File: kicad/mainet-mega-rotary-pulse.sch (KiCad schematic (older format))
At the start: 11 parts, among them J65 Screw_Terminal_01x02, J66 Screw_Terminal_01x04, Q1 BUK9518-55, U1 4N38

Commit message: KICAD: Modificar sch del RPG
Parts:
- added J100, J99: Conn_01x01_Male, symbol Connector:Conn_01x01_Male
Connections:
- net labels removed: rotaryPulseOutput24V
- wire segments 30 -> 36
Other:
- note added: "+24V"
- note added: "Blanco"
- note added: "Esta señal es la salida a colector abierto\ndel RPG (Rotary Pulse Generator),\ngenerador de pulsos por rotación,\na 24VDC\n"
- note added: "Esta señal es la salida del generafor\nde pulsos por rotación trasladada a 5V.\nVa a la entrada D24 del Arduino-Mega"
- note added: "RPG"
- note added: "RPG Output"
- note added: "Rojo"
- note removed: "Esta señal es la salida del generador \nde pulsos por rotación a 24VDC\n"
- note removed: "Esta señal es la salida del generafor\nde pulsos por rotación trasladada a 5V"
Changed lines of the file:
@@
 $Descr A4 11693 8268
 encoding utf-8
-Sheet 21 22
+Sheet 22 22
 Title "Mainet-mega -- Convertidor de Voltaje: 24V a 5V"
 Date "2021-06-25"
@@
 Comment4 ""
 $EndDescr
-Text HLabel 3550 3750 2    50   Input ~ 0
-rotaryPulseOutput24V
+Text HLabel 6800 3600 2    50   Input ~ 0
+rotaryPulseOutput5V
 $Comp
 L Transistor_FET:IRLZ44N Q1
@@
 	6700 4050 6700 4450
 Connection ~ 6700 4450
-Text Label 7650 3600 2    50   ~ 0
-rotaryPulseOutput5V
 Text Label 6700 4450 0    50   ~ 0
 0V
-Text Notes 1350 3800 0    50   ~ 0
-Esta señal es la salida del generador \nde pulsos por rotación a 24VDC\n
-Text Notes 9100 3650 0    50   ~ 0
-Esta señal es la salida del generafor\nde pulsos por rotación trasladada a 5V
+Text Notes 3550 4300 0    50   ~ 0
+Esta señal es la salida a colector abierto\ndel RPG (Rotary Pulse Generator),\ngenerador de pulsos por rotación,\na 24VDC\n
+Text Notes 9150 3900 0    50   ~ 0
+Esta señal es la salida del generafor\nde pulsos por rotación trasladada a 5V.\nVa a la entrada D24 del Arduino-Mega
 $Comp
 L power:GNDD #PWR040
@@
 Wire Wire Line
 	4600 3050 5000 3050
+Text Notes 6500 5900 0    50   ~ 0
++24V
+Text Notes 3550 3750 0    50   ~ 0
++24V
+Text Notes 3550 3850 0    50   ~ 0
+RPG Output
+$Comp
+L Connector:Conn_01x01_Male J99
+U 1 1 60DC2EE7
+P 2600 3750
+F 0 "J99" H 2700 3650 50  0000 R CNN
+F 1 "Conn_01x01_Male" H 2572 3773 50  0001 R CNN
+F 2 "" H 2600 3750 50  0001 C CNN
+F 3 "~" H 2600 3750 50  0001 C CNN
+	1    2600 3750
+	-1   0    0    1
+$EndComp
+$Comp
+L Connector:Conn_01x01_Male J100
+U 1 1 60DC43F7
+P 2600 3850
+F 0 "J100" H 2750 3950 50  0000 R CNN
+F 1 "Conn_01x01_Male" H 2572 3873 50  0001 R CNN
+F 2 "" H 2600 3850 50  0001 C CNN
+F 3 "~" H 2600 3850 50  0001 C CNN
+	1    2600 3850
+	-1   0    0    1
+$EndComp
+Wire Notes Line
+	800  3900 1700 3900
+Wire Notes Line
+	1700 3900 1700 4700
+Wire Notes Line
+	1700 4700 800  4700
+Wire Notes Line
+	800  4700 800  3900
+Text Notes 900  4000 0    50   ~ 0
+RPG
+Wire Wire Line
+	1250 3900 1250 3750
+Wire Wire Line
+	1250 3750 2400 3750
+Wire Wire Line
+	2400 3850 1850 3850
+Wire Wire Line
+	1850 3850 1850 4250
+Wire Wire Line
+	1850 4250 1550 4250
+Wire Wire Line
+	1250 4700 1250 4850
+Text Notes 1850 3750 0    50   ~ 0
+Rojo
+Text Notes 1850 3850 0    50   ~ 0
+Blanco
 $EndSCHEMATC

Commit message: KICAD: Actualizar archivos sch
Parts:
- added J102: Conector del RPG, symbol Connector:Screw_Terminal_01x04
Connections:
- net labels added: +24V, GNDREF
- no-connect marks 1 -> 2
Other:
- note added: "Negro"
- note added: "Puede ser cualquiera de las salidas de +5V del Arduino-Mega"
- note removed: "No es la salida de +5V del Arduino"
- note removed: "RPG"
- moved on the sheet: D21, D22, D23, J65, J66, Q9, R17, R18, R19, R20, U10

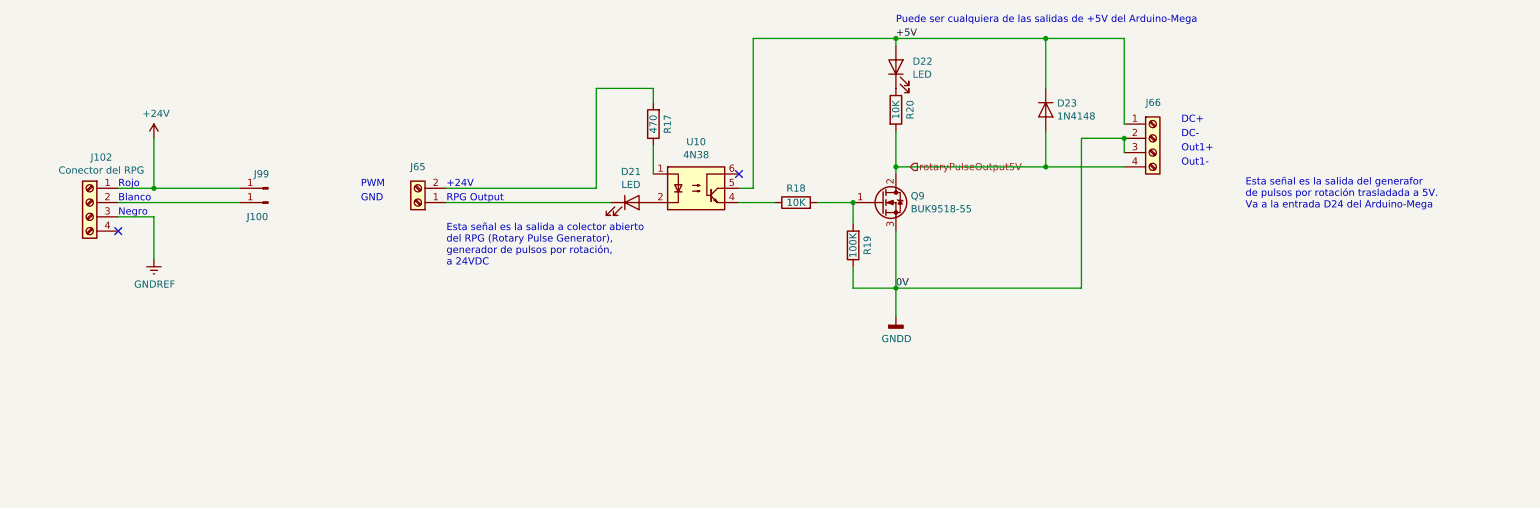
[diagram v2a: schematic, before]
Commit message: KICAD: Corregir pinout conector RPG
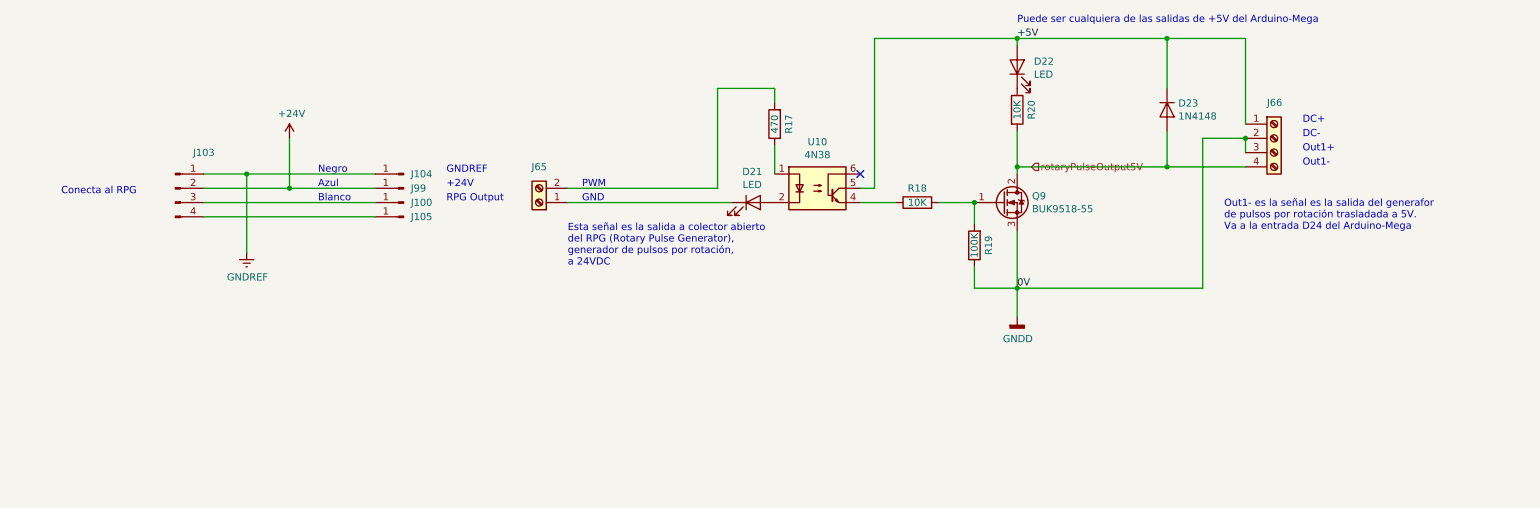
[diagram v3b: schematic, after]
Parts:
- removed J102: Conector del RPG, symbol Connector:Screw_Terminal_01x04
- added J103: Conn_01x04_Male, symbol Connector:Conn_01x04_Male
- added J104, J105: Conn_01x01_Male, symbol Connector:Conn_01x01_Male
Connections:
- net +24V: now also J103.2 (Pin_2)
- net GNDREF: now also J103.1 (Pin_1), J104.1 (Pin_1)
- net at J100.1 (Pin_1): now also J103.3 (Pin_3)
- new net: J103.4 (Pin_4), J105.1 (Pin_1)
- no-connect marks 2 -> 1
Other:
- note added: "Azul"
- note added: "Conecta al RPG"
- note added: "GNDREF\n"
- note added: "Out1- es la señal es la salida del generafor\nde pulsos por rotación trasladada a 5V.\nVa a la entrada D24 del Arduino-Mega"
- note removed: "Esta señal es la salida del generafor\nde pulsos por rotación trasladada a 5V.\nVa a la entrada D24 del Arduino-Mega"
- note removed: "Rojo"
- moved on the sheet: D21, D22, D23, J100, J65, J66, J99, Q9, R17, R18, R19, R20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

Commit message: KICAD: Agregar correcciones en .sch
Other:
- note added: "(+24V)"
- note added: "(RPG Output)"
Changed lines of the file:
@@
 	2150 3850 3350 3850
-Wire Wire Line
-	2150 3950 3350 3950
 Wire Wire Line
 	2450 3650 2450 4200
@@
 Text Notes 1150 3800 0    50   ~ 0
 Conecta al RPG
+Text Notes 5000 3750 0    50   ~ 0
+(+24V)
+Text Notes 5000 3850 0    50   ~ 0
+(RPG Output)
+Wire Wire Line
+	2150 3950 3350 3950
 $EndSCHEMATC

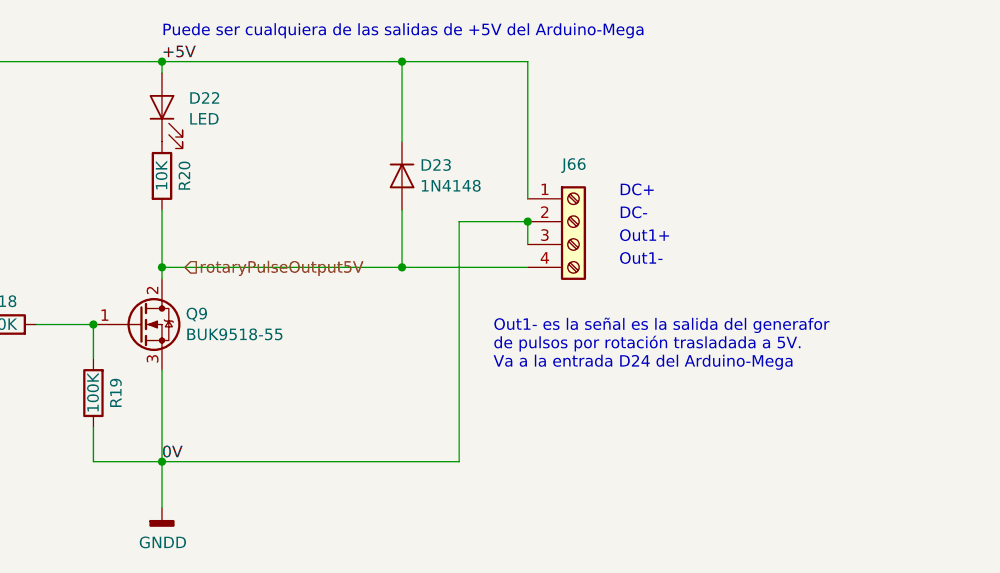
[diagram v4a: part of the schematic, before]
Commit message: KICAD: Agegar cambios en .sch de mainet-mega-rotary-pulse.sch
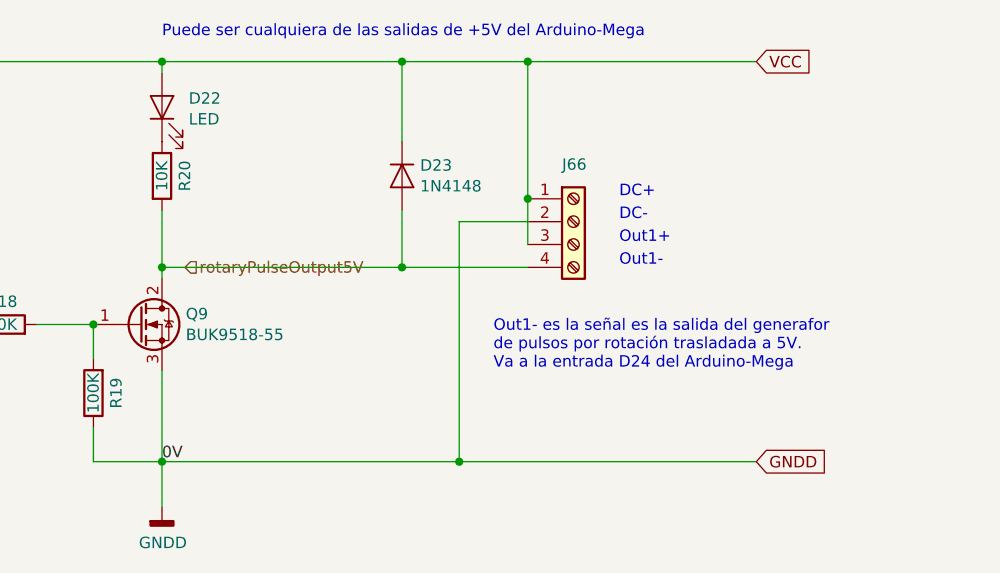
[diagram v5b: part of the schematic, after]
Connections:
- net GNDD: no longer J66.3 (Pin_3)
- net +5V renamed VCC
- net VCC: now also J66.3 (Pin_3)
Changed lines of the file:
@@
 Wire Wire Line
 	6750 3850 7000 3850
-Text Label 7850 2700 0    50   ~ 0
-+5V
 Wire Wire Line
 	7550 4300 7550 4450
@@
 Wire Wire Line
 	2750 3750 3350 3750
-Connection ~ 9450 3400
-Wire Wire Line
-	9450 3400 9450 3500
 Text Notes 2950 3650 0    50   ~ 0
 Negro
@@
 Wire Wire Line
 	2150 3950 3350 3950
+Text GLabel 10450 4450 2    50   Input ~ 0
+GNDD
+Text GLabel 10450 2700 2    50   Input ~ 0
+VCC
+Wire Wire Line
+	9450 2700 10450 2700
+Connection ~ 9450 2700
+Wire Wire Line
+	10450 4450 9150 4450
+Connection ~ 9150 4450
+Connection ~ 9450 3300
+Wire Wire Line
+	9450 3300 9450 3500
 $EndSCHEMATC

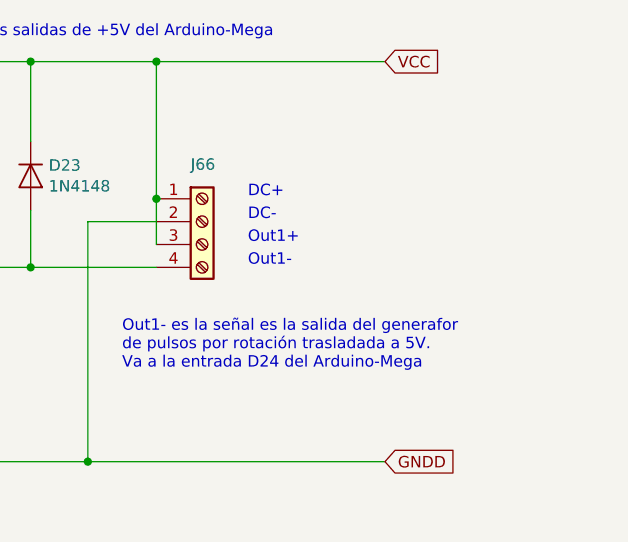
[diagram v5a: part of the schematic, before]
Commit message: KICAD: Guardar cambios en sch RPG
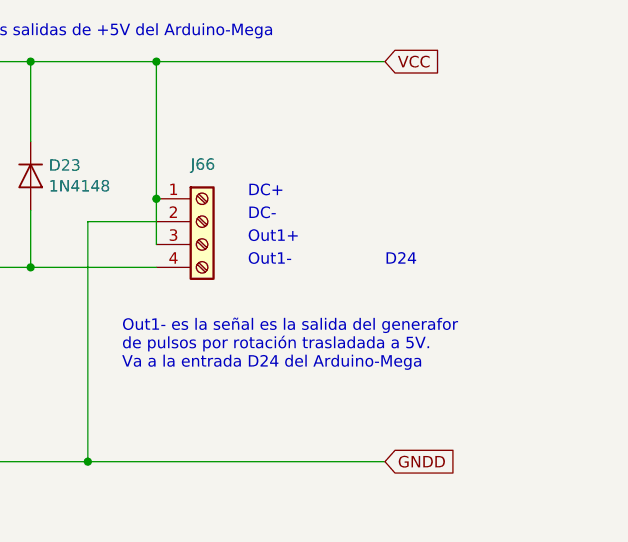
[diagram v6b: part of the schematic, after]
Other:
- note added: "D24"
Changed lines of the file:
@@
 Sheet 22 22
 Title "Mainet-mega -- Convertidor de Voltaje: 24V a 5V"
-Date "2021-06-25"
+Date "2021-07-13"
 Rev "1.0"
 Comp "Tovenca"
@@
 Wire Wire Line
 	9450 3300 9450 3500
+Text Notes 10450 3600 0    50   ~ 0
+D24
 $EndSCHEMATC
